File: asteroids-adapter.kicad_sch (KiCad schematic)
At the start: 16 parts, among them J1 Asteroids PCB connector, J2 Asteroids harness connector, U1 TL074

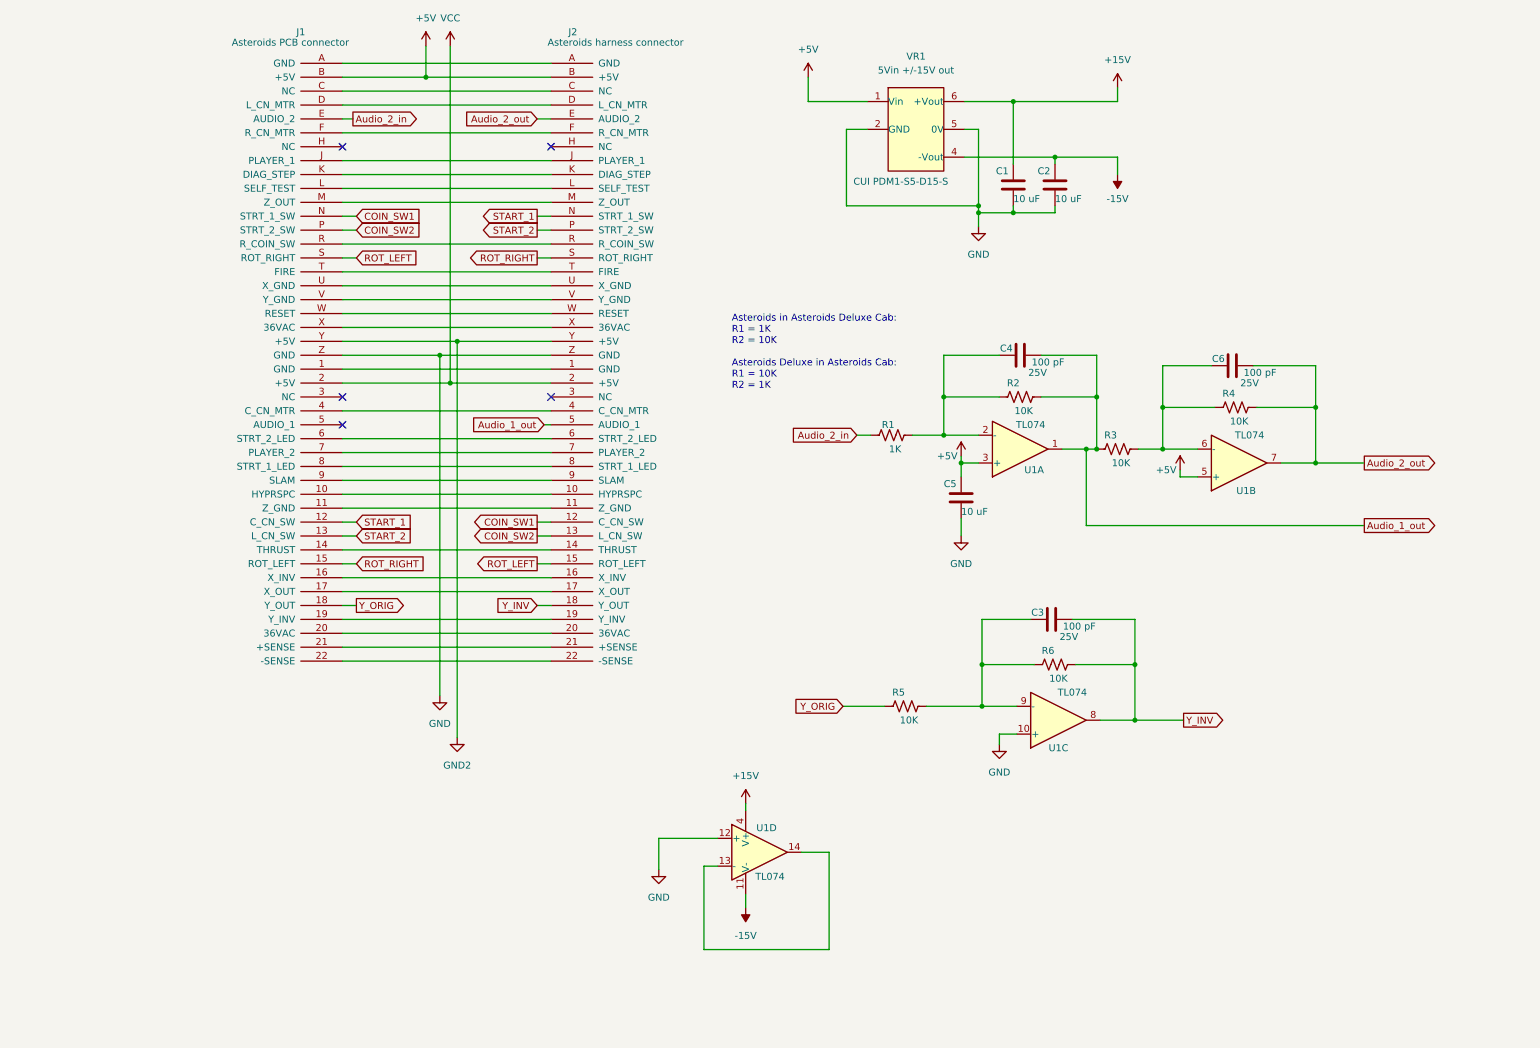
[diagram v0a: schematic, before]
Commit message: Add jumper for configuration
Configure unused opamp as 0.1x gain, and add jumper to select between
10x and 0.1x gain audio.
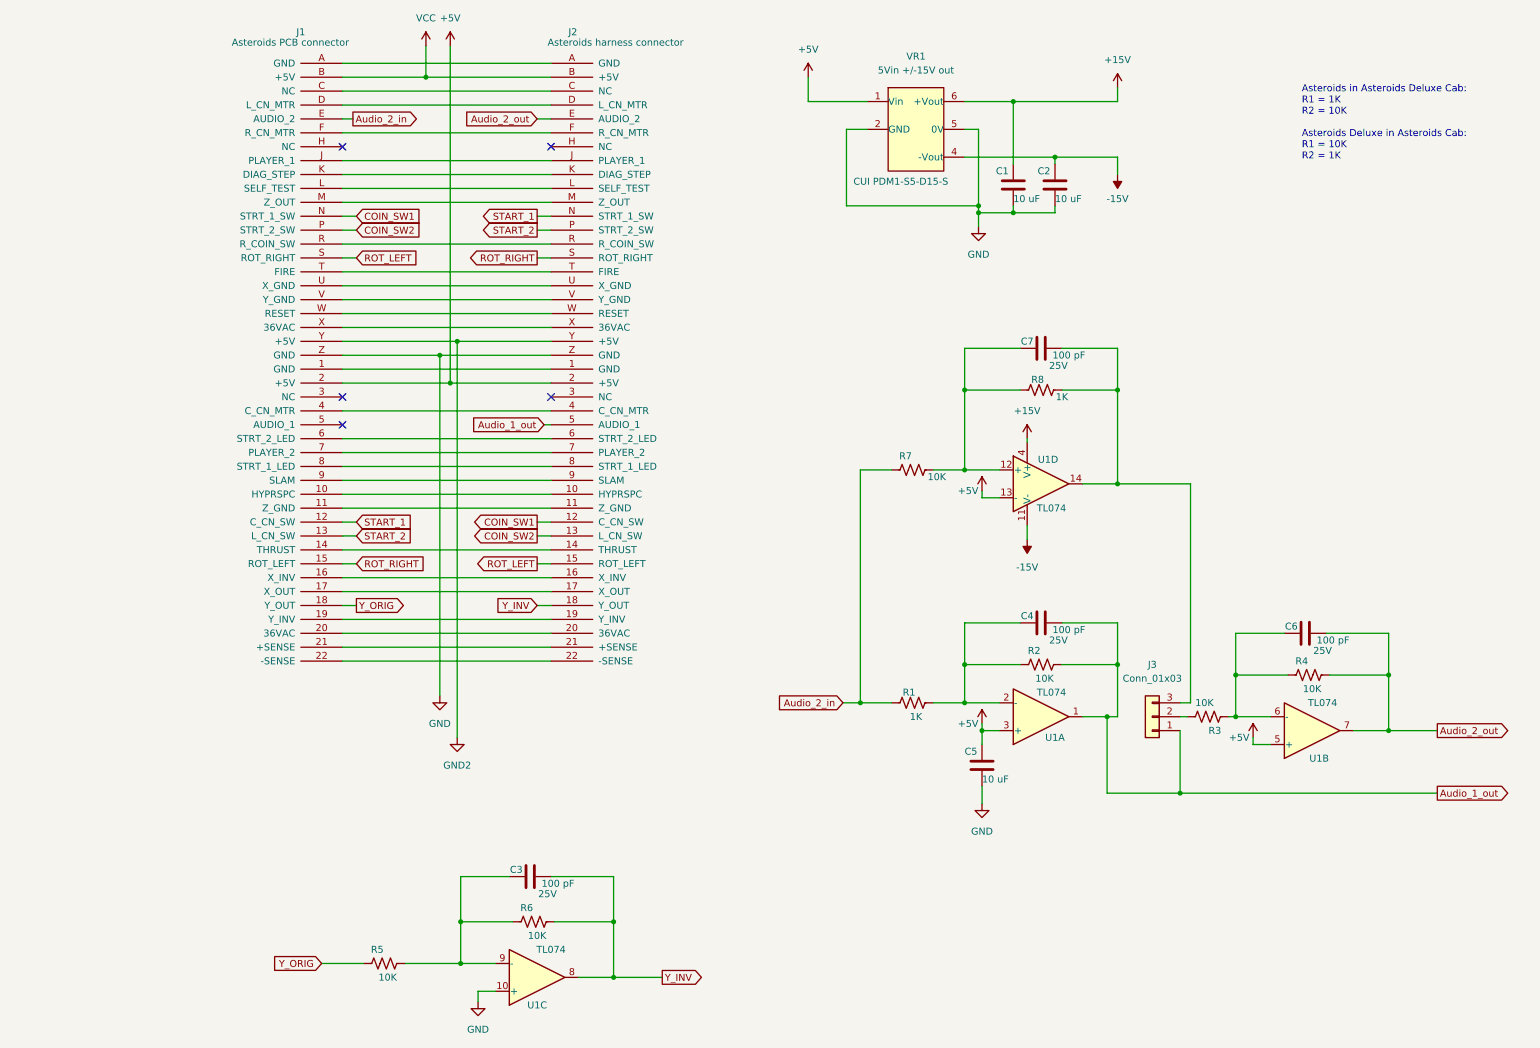
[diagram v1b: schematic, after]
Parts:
- added C7: Kemet MLCC 100 pF 5% 25V TH, Capacitor_THT:C_Disc_D3.0mm_W1.6mm_P2.50mm, symbol ast-adapter: Kemet MLCC 100 pF 5% 25V TH
- added J3: Conn_01x03, Connector_PinHeader_1.00mm:PinHeader_1x03_P1.00mm_Vertical, symbol Connector_Generic:Conn_01x03
- added R7: Yageo 10K ohm 1% thin film TH, Resistor_THT:R_Axial_DIN0207_L6.3mm_D2.5mm_P10.16mm_Horizontal, symbol ast-adapter:Yageo 10K ohm 1% thin film TH
- added R8: Yageo 1K ohm 1% thin film TH, Resistor_THT:R_Axial_DIN0207_L6.3mm_D2.5mm_P10.16mm_Horizontal, symbol ast-adapter:Yageo 1K ohm 1% thin film TH
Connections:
- net +5V: now also J1.2 (+5V), J2.2 (+5V), U1.13 (-); no longer J1.B (+5V), J2.B (+5V)
- net Audio_1_out: now also J3.1 (Pin_1); no longer R3.2
- net Audio_2_in: now also R7.2
- net GND: no longer U1.12 (+)
- net VCC: now also J1.B (+5V), J2.B (+5V); no longer J1.2 (+5V), J2.2 (+5V)
- net at C6.1, R4.2, U1.6 (-): now also R3.2; no longer R3.1
- net at U1.14: now also C7.2, J3.3 (Pin_3), R8.1; no longer U1.13 (-)
- new net: C7.1, R7.1, R8.2, U1.12 (+)
- new net: J3.2 (Pin_2), R3.1
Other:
- moved on the sheet: C3, C4, C5, C6, R1, R2, R3, R4, R5, R6, U1A, U1B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

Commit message: Fixed jumper to 0.1" 3-pin header
also silk screen fixed
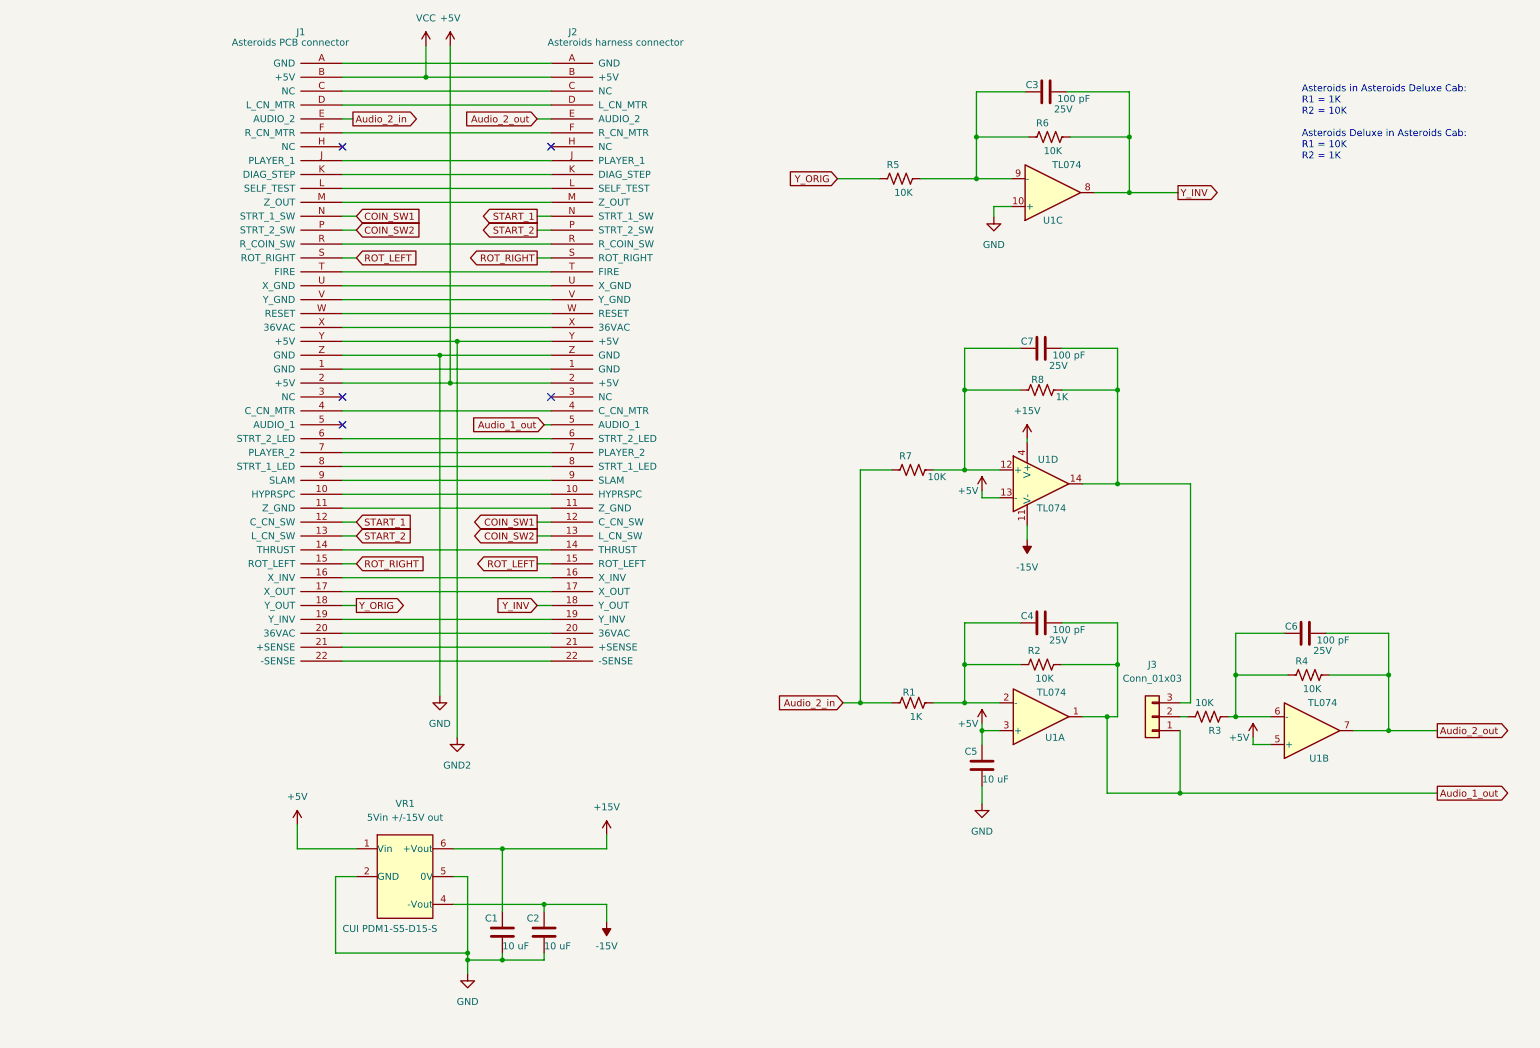
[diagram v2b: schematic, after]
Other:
- moved on the sheet: C1, C2, C3, R5, R6, U1C, VR1

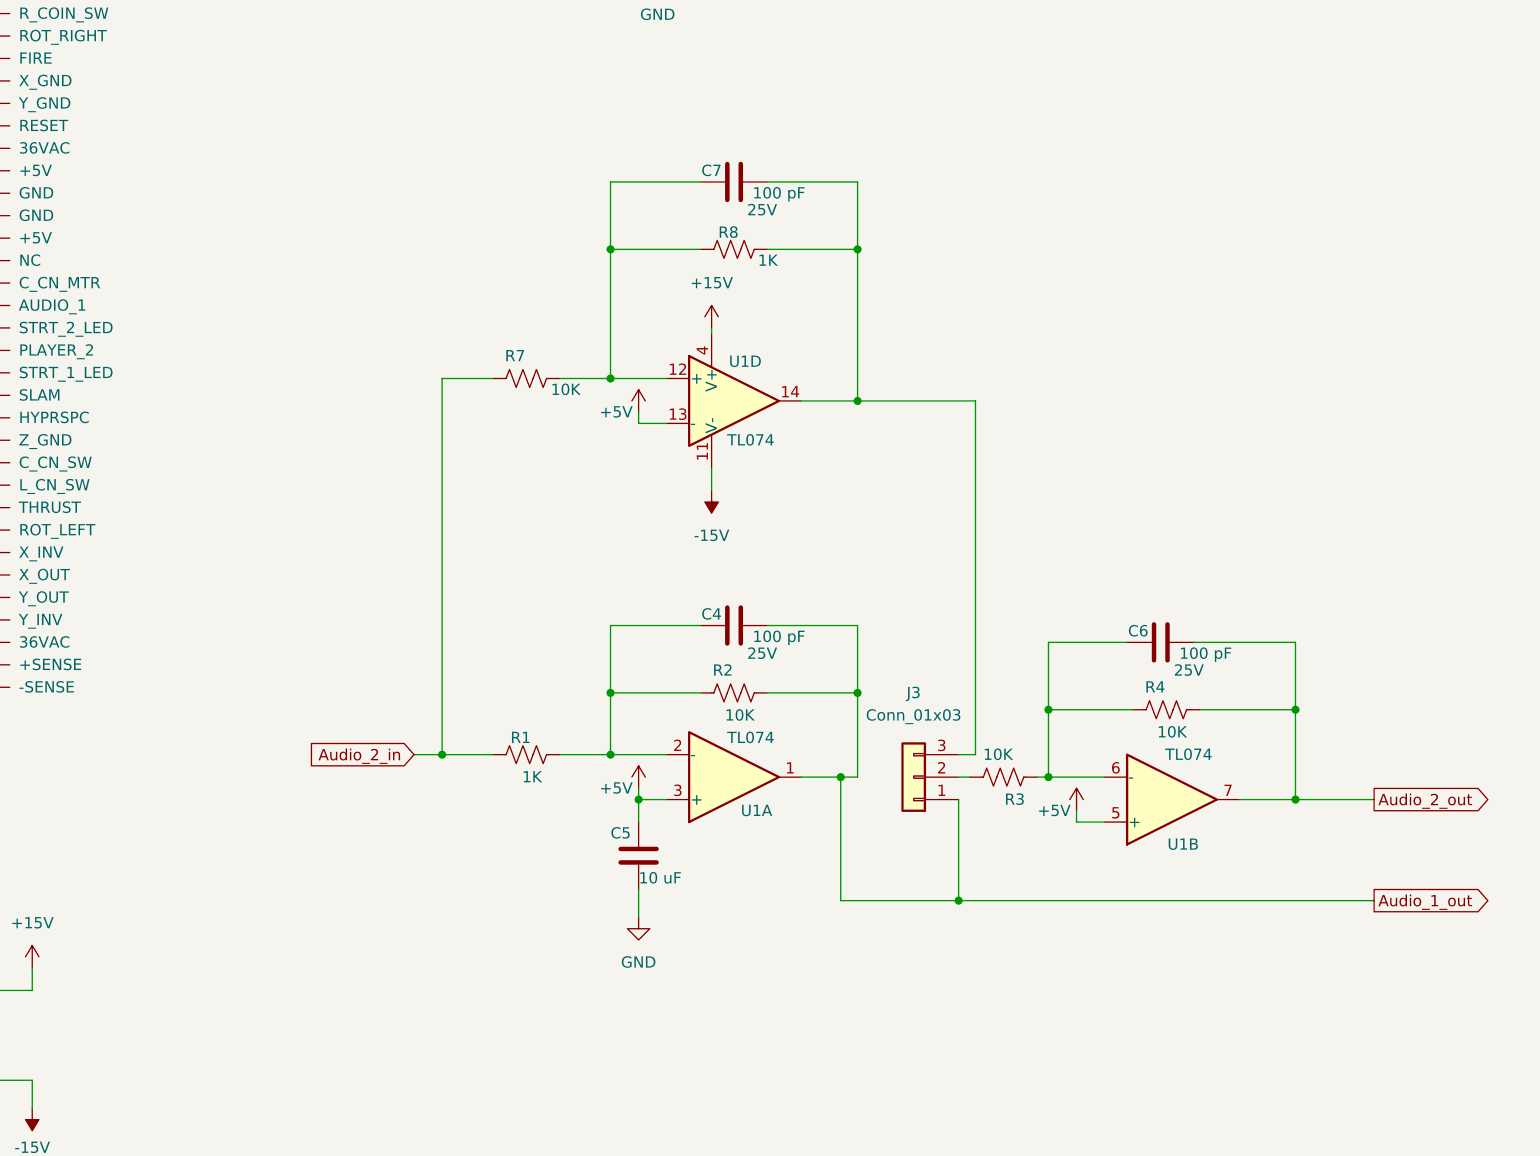
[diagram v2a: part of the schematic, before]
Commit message: Fixed audio output selection
Audio 1 was always connected to the x10 gain amplifier, instead of the
gain selected by the jumper.

Also, fixed the 3-pin header in the schematic to use the correct 2.54mm
pitch part.
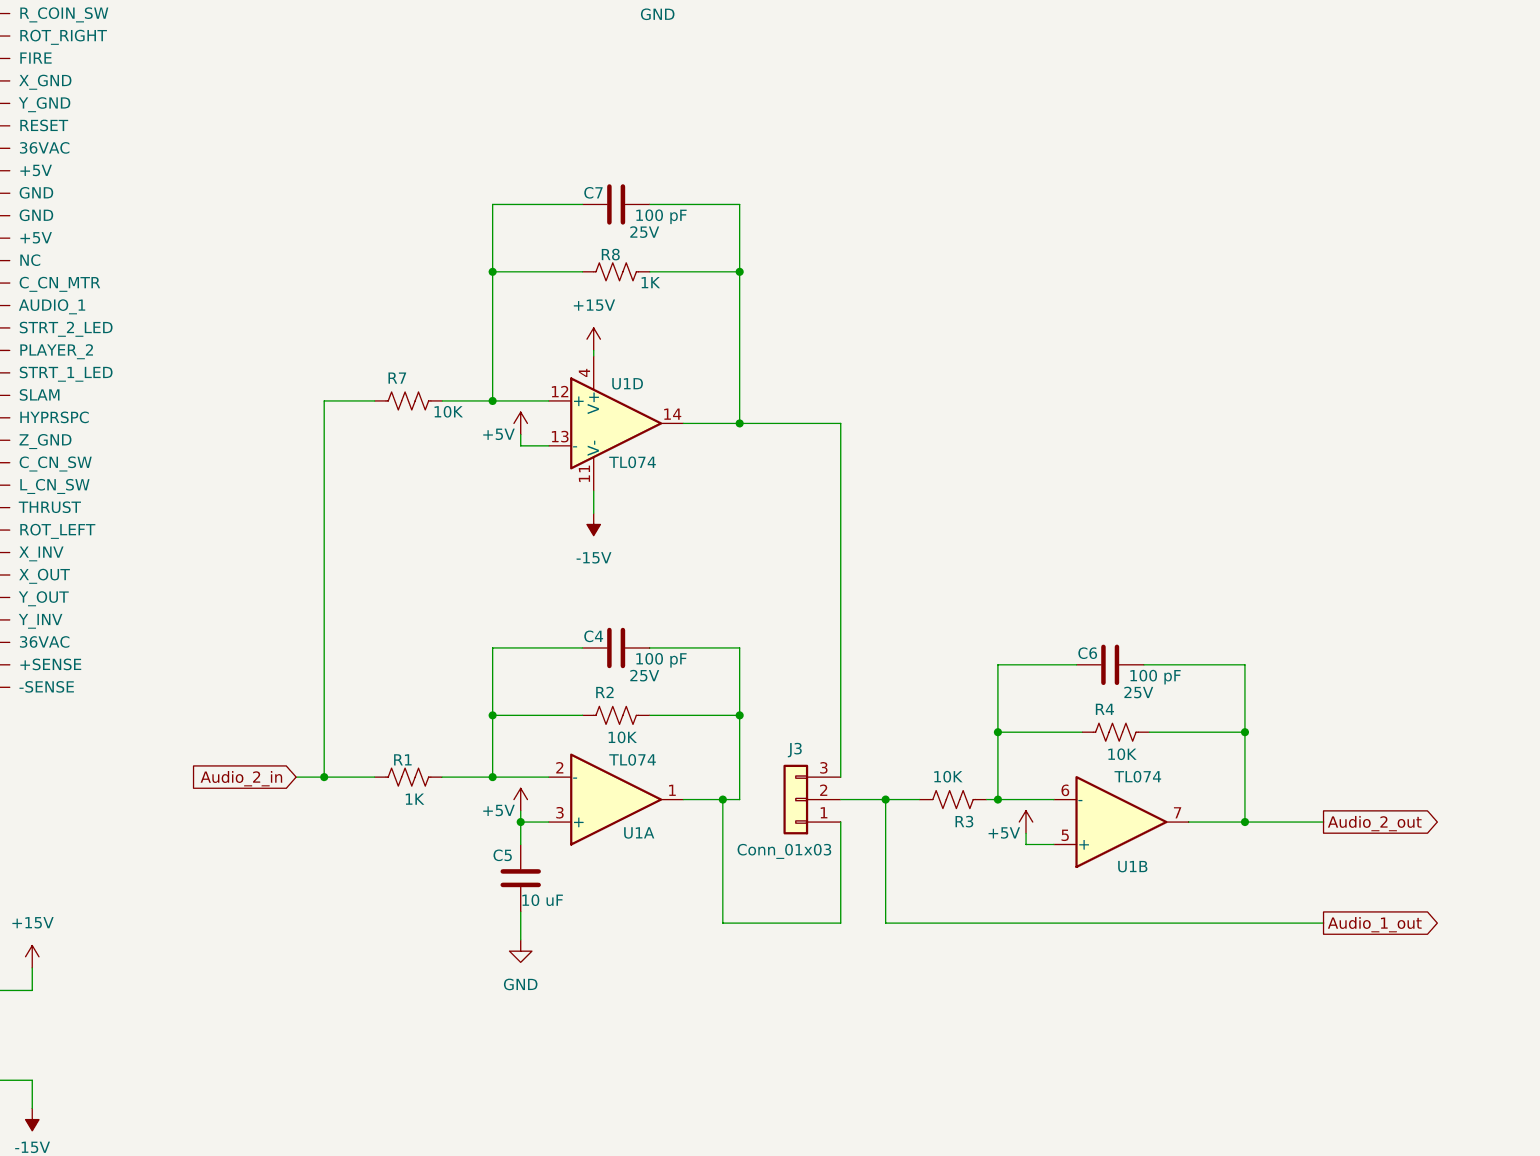
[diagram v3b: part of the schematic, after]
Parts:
- J3: footprint Connector_PinHeader_1.00mm:PinHeader_1x03_P1.00mm_Vertical -> Connector_PinHeader_2.54mm:PinHeader_1x03_P2.54mm_Vertical
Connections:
- net Audio_1_out: now also J3.2 (Pin_2), R3.1; no longer C4.2, J3.1 (Pin_1), R2.1, U1.1
- new net: C4.2, J3.1 (Pin_1), R2.1, U1.1
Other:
- moved on the sheet: C4, C5, C6, C7, J3, R1, R2, R3, R4, R7, R8, U1A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
